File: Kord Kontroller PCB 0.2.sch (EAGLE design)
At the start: 188 parts, among them IC2 74HCT1G125DBV, J1 MIDIOUTB, J2 MIDIOUTA, J3 FTSH-105-01-L-DV-KJ, SW2 SPST_TACT-KMR2, U1 AP2112K-3.3, U2 ATSAMD51J19A-AUT, X3 microUSB

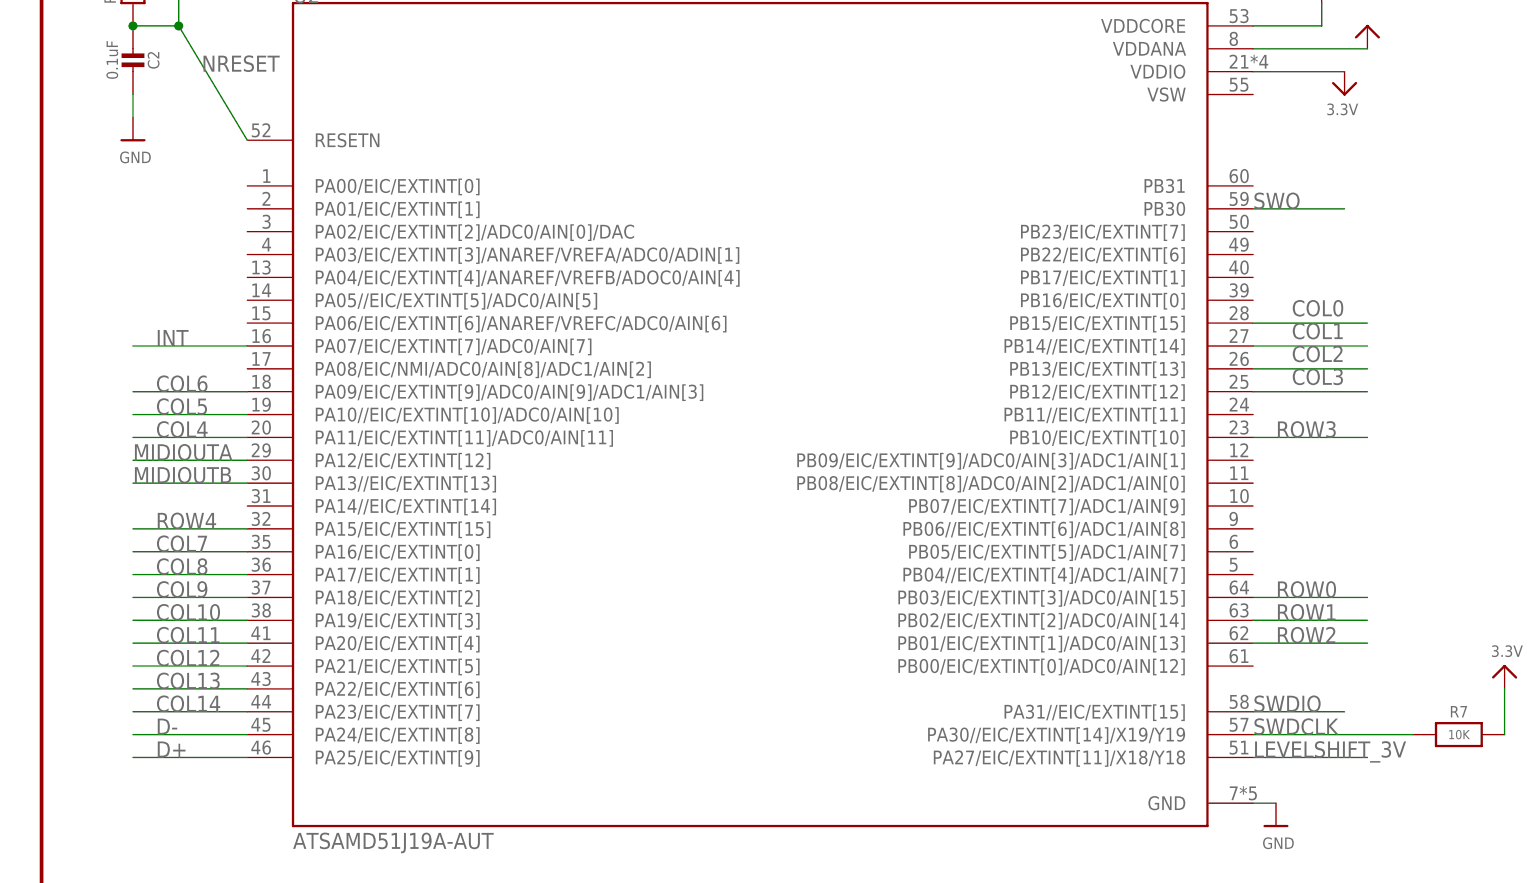
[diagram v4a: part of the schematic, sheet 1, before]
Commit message: Added traces for 7-14
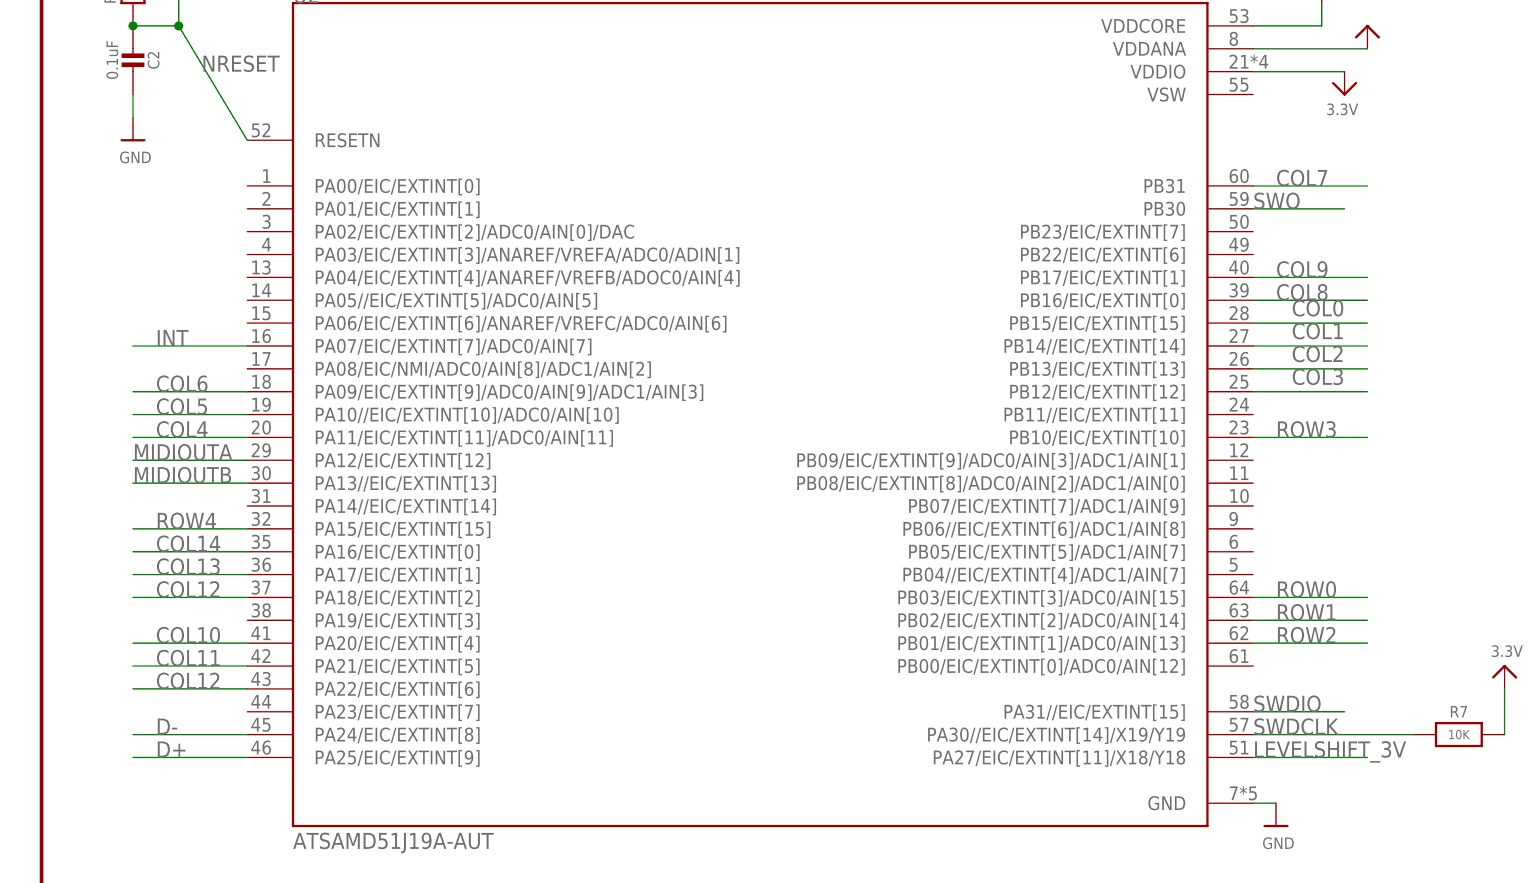
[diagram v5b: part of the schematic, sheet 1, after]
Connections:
- net COL10: now also U2.PA20/EIC/EXTINT[4]; no longer U2.PA19/EIC/EXTINT[3]
- net COL11: now also U2.PA21/EIC/EXTINT[5]; no longer U2.PA20/EIC/EXTINT[4]
- net COL12: now also U2.PA18/EIC/EXTINT[2], U2.PA22/EIC/EXTINT[6]; no longer U2.PA21/EIC/EXTINT[5]
- net COL13: now also U2.PA17/EIC/EXTINT[1]; no longer U2.PA22/EIC/EXTINT[6]
- net COL14: now also U2.PA16/EIC/EXTINT[0]; no longer U2.PA23/EIC/EXTINT[7]
- net COL7: now also B29.P$1, U2.PB31; no longer U2.PA16/EIC/EXTINT[0]
- net COL8: now also U2.PB16/EIC/EXTINT[0]; no longer B29.P$1, U2.PA17/EIC/EXTINT[1]
- net COL9: now also U2.PB17/EIC/EXTINT[1]; no longer U2.PA18/EIC/EXTINT[2]
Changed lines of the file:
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@@
 <net name="COL7" class="0">
 <segment>
-<wire x1="652.78" y1="-63.5" x2="665.48" y2="-63.5" width="0.1524" layer="91"/>
-<label x="655.32" y="-63.5" size="1.778" layer="95"/>
-<pinref part="U2" gate="G$1" pin="PA16/EIC/EXTINT[0]"/>
+<wire x1="777.24" y1="-22.86" x2="789.94" y2="-22.86" width="0.1524" layer="91"/>
+<label x="779.78" y="-22.86" size="1.778" layer="95"/>
+<pinref part="U2" gate="G$1" pin="PB31"/>
 </segment>
 </net>
@@
 <net name="COL8" class="0">
 <segment>
-<wire x1="665.48" y1="-66.04" x2="652.78" y2="-66.04" width="0.1524" layer="91"/>
-<label x="655.32" y="-66.04" size="1.778" layer="95"/>
-<pinref part="U2" gate="G$1" pin="PA17/EIC/EXTINT[1]"/>
+<wire x1="789.94" y1="-35.56" x2="777.24" y2="-35.56" width="0.1524" layer="91"/>
+<label x="779.78" y="-35.56" size="1.778" layer="95"/>
+<pinref part="U2" gate="G$1" pin="PB16/EIC/EXTINT[0]"/>
 </segment>
 </net>
 <net name="COL9" class="0">
+<segment>
+<wire x1="777.24" y1="-33.02" x2="789.94" y2="-33.02" width="0.1524" layer="91"/>
+<label x="779.78" y="-33.02" size="1.778" layer="95"/>
+<pinref part="U2" gate="G$1" pin="PB17/EIC/EXTINT[1]"/>
+</segment>
+</net>
+<net name="COL10" class="0">
+<segment>
+<wire x1="652.78" y1="-73.66" x2="665.48" y2="-73.66" width="0.1524" layer="91"/>
+<label x="655.32" y="-73.66" size="1.778" layer="95"/>
+<pinref part="U2" gate="G$1" pin="PA20/EIC/EXTINT[4]"/>
+</segment>
+</net>
+<net name="COL11" class="0">
+<segment>
+<wire x1="652.78" y1="-76.2" x2="665.48" y2="-76.2" width="0.1524" layer="91"/>
+<label x="655.32" y="-76.2" size="1.778" layer="95"/>
+<pinref part="U2" gate="G$1" pin="PA21/EIC/EXTINT[5]"/>
+</segment>
+</net>
+<net name="COL12" class="0">
 <segment>
 <wire x1="652.78" y1="-68.58" x2="665.48" y2="-68.58" width="0.1524" layer="91"/>
@@
 <pinref part="U2" gate="G$1" pin="PA18/EIC/EXTINT[2]"/>
 </segment>
-</net>
-<net name="COL10" class="0">
-<segment>
-<wire x1="652.78" y1="-71.12" x2="665.48" y2="-71.12" width="0.1524" layer="91"/>
-<label x="655.32" y="-71.12" size="1.778" layer="95"/>
-<pinref part="U2" gate="G$1" pin="PA19/EIC/EXTINT[3]"/>
-</segment>
-</net>
-<net name="COL11" class="0">
-<segment>
-<wire x1="652.78" y1="-73.66" x2="665.48" y2="-73.66" width="0.1524" layer="91"/>
-<label x="655.32" y="-73.66" size="1.778" layer="95"/>
-<pinref part="U2" gate="G$1" pin="PA20/EIC/EXTINT[4]"/>
-</segment>
-</net>
-<net name="COL12" class="0">
-<segment>
-<wire x1="652.78" y1="-76.2" x2="665.48" y2="-76.2" width="0.1524" layer="91"/>
-<label x="655.32" y="-76.2" size="1.778" layer="95"/>
-<pinref part="U2" gate="G$1" pin="PA21/EIC/EXTINT[5]"/>
-</segment>
-</net>
-<net name="COL13" class="0">
 <segment>
 <wire x1="652.78" y1="-78.74" x2="665.48" y2="-78.74" width="0.1524" layer="91"/>
@@
 </segment>
 </net>
+<net name="COL13" class="0">
+<segment>
+<wire x1="652.78" y1="-66.04" x2="665.48" y2="-66.04" width="0.1524" layer="91"/>
+<label x="655.32" y="-66.04" size="1.778" layer="95"/>
+<pinref part="U2" gate="G$1" pin="PA17/EIC/EXTINT[1]"/>
+</segment>
+</net>
 <net name="COL14" class="0">
 <segment>
-<wire x1="652.78" y1="-81.28" x2="665.48" y2="-81.28" width="0.1524" layer="91"/>
-<label x="655.32" y="-81.28" size="1.778" layer="95"/>
-<pinref part="U2" gate="G$1" pin="PA23/EIC/EXTINT[7]"/>
+<wire x1="652.78" y1="-63.5" x2="665.48" y2="-63.5" width="0.1524" layer="91"/>
+<label x="655.32" y="-63.5" size="1.778" layer="95"/>
+<pinref part="U2" gate="G$1" pin="PA16/EIC/EXTINT[0]"/>
 </segment>
 </net>
@@
 <pinref part="B28" gate="G$1" pin="P$1"/>
 <junction x="139.7" y="193.04"/>
+<wire x1="170.18" y1="193.04" x2="185.42" y2="193.04" width="0.1524" layer="91"/>
+<junction x="170.18" y="193.04"/>
+<pinref part="B29" gate="G$1" pin="P$1"/>
+<wire x1="185.42" y1="198.12" x2="185.42" y2="193.04" width="0.1524" layer="91"/>
 </segment>
 </net>
@@
 <wire x1="147.32" y1="198.12" x2="147.32" y2="187.96" width="0.1524" layer="91"/>
 <junction x="147.32" y="187.96"/>
-<pinref part="B29" gate="G$1" pin="P$1"/>
-<wire x1="185.42" y1="198.12" x2="185.42" y2="187.96" width="0.1524" layer="91"/>
-<wire x1="185.42" y1="187.96" x2="177.8" y2="187.96" width="0.1524" layer="91"/>
-<junction x="177.8" y="187.96"/>
-</segment>
-</net>
+</segment>
+</net>

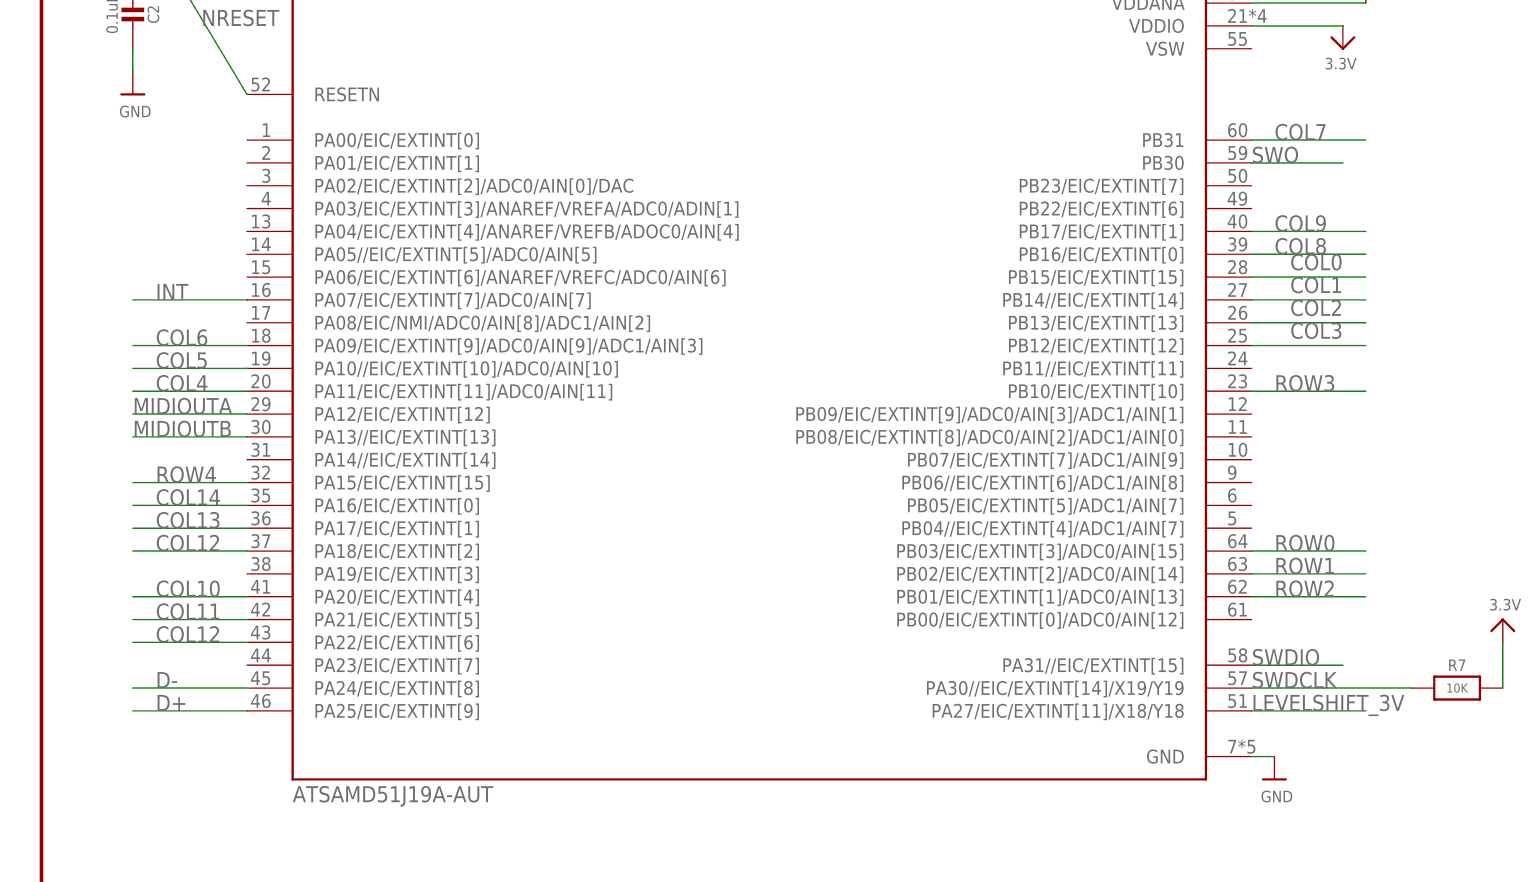
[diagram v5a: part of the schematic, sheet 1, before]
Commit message: routed power and midi
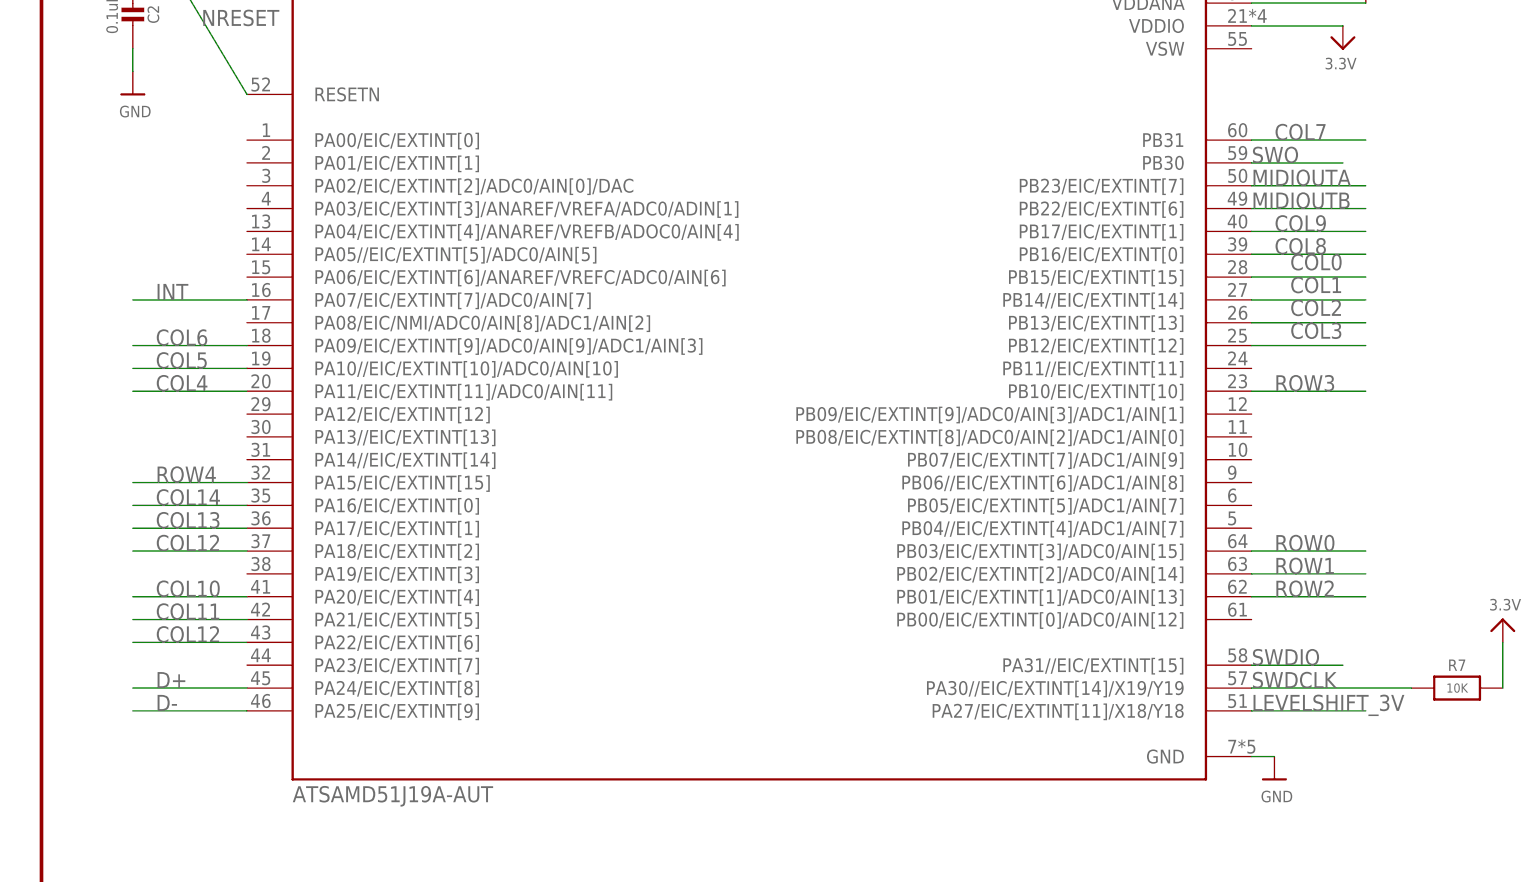
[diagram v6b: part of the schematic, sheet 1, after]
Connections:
- net D+: now also U2.PA24/EIC/EXTINT[8]; no longer U2.PA25/EIC/EXTINT[9]
- net D-: now also U2.PA25/EIC/EXTINT[9]; no longer U2.PA24/EIC/EXTINT[8]
- net MIDIOUTA: now also U2.PB23/EIC/EXTINT[7]; no longer U2.PA12/EIC/EXTINT[12]
- net MIDIOUTB: now also U2.PB22/EIC/EXTINT[6]; no longer U2.PA13//EIC/EXTINT[13]
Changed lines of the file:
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@@
 </segment>
 <segment>
-<wire x1="665.48" y1="-86.36" x2="652.78" y2="-86.36" width="0.1524" layer="91"/>
-<label x="655.32" y="-86.36" size="1.778" layer="95"/>
-<pinref part="U2" gate="G$1" pin="PA25/EIC/EXTINT[9]"/>
+<wire x1="665.48" y1="-83.82" x2="652.78" y2="-83.82" width="0.1524" layer="91"/>
+<label x="655.32" y="-83.82" size="1.778" layer="95"/>
+<pinref part="U2" gate="G$1" pin="PA24/EIC/EXTINT[8]"/>
 </segment>
 </net>
@@
 </segment>
 <segment>
-<wire x1="652.78" y1="-83.82" x2="665.48" y2="-83.82" width="0.1524" layer="91"/>
-<label x="655.32" y="-83.82" size="1.778" layer="95"/>
-<pinref part="U2" gate="G$1" pin="PA24/EIC/EXTINT[8]"/>
+<wire x1="652.78" y1="-86.36" x2="665.48" y2="-86.36" width="0.1524" layer="91"/>
+<label x="655.32" y="-86.36" size="1.778" layer="95"/>
+<pinref part="U2" gate="G$1" pin="PA25/EIC/EXTINT[9]"/>
 </segment>
 </net>
@@
 </segment>
 <segment>
-<wire x1="652.78" y1="-53.34" x2="665.48" y2="-53.34" width="0.1524" layer="91"/>
-<label x="652.78" y="-53.34" size="1.778" layer="95"/>
-<pinref part="U2" gate="G$1" pin="PA12/EIC/EXTINT[12]"/>
+<wire x1="777.24" y1="-27.94" x2="789.94" y2="-27.94" width="0.1524" layer="91"/>
+<label x="777.24" y="-27.94" size="1.778" layer="95"/>
+<pinref part="U2" gate="G$1" pin="PB23/EIC/EXTINT[7]"/>
 </segment>
 </net>
@@
 </segment>
 <segment>
-<wire x1="652.78" y1="-55.88" x2="665.48" y2="-55.88" width="0.1524" layer="91"/>
-<label x="652.78" y="-55.88" size="1.778" layer="95"/>
-<pinref part="U2" gate="G$1" pin="PA13//EIC/EXTINT[13]"/>
+<wire x1="777.24" y1="-30.48" x2="789.94" y2="-30.48" width="0.1524" layer="91"/>
+<label x="777.24" y="-30.48" size="1.778" layer="95"/>
+<pinref part="U2" gate="G$1" pin="PB22/EIC/EXTINT[6]"/>
 </segment>
 </net>

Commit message: Added VDD plane and GND plane
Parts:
- removed FRAME1: FRAME-LEDGER, SparkFun-Aesthetics:FRAME-LEDGER
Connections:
- net COL12: no longer U2.PA18/EIC/EXTINT[2]
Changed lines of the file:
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@@
 <part name="GND18" library="supply1" deviceset="GND" device=""/>
 <part name="GND19" library="supply1" deviceset="GND" device=""/>
-<part name="FRAME1" library="SparkFun-Aesthetics" deviceset="FRAME-LEDGER" device=""/>
 <part name="D25" library="microbuilder" deviceset="DIODE" device="SOD-323" value="1N4148"/>
 <part name="D33" library="microbuilder" deviceset="DIODE" device="SOD-323" value="1N4148"/>
@@
 <attribute name="VALUE" x="706.12" y="55.88" size="1.778" layer="96"/>
 </instance>
-<instance part="FRAME1" gate="G$1" x="642.62" y="-106.68" smashed="yes"/>
-<instance part="FRAME1" gate="G$2" x="972.82" y="-106.68" smashed="yes">
-<attribute name="LAST_DATE_TIME" x="985.52" y="-105.41" size="2.54" layer="94" font="vector"/>
-<attribute name="SHEET" x="1059.18" y="-105.41" size="2.54" layer="94" font="vector"/>
-<attribute name="DRAWING_NAME" x="988.314" y="-88.9" size="2.7432" layer="94" font="vector"/>
-<attribute name="DESIGNER" x="995.934" y="-95.504" size="2.7432" layer="94" font="vector"/>
-<attribute name="REV" x="1061.72" y="-100.076" size="2.7432" layer="94" font="vector"/>
-</instance>
 <instance part="R5" gate="G$1" x="835.66" y="78.74" smashed="yes">
 <attribute name="NAME" x="831.85" y="80.2386" size="1.778" layer="95"/>
@@
 <net name="COL12" class="0">
 <segment>
-<wire x1="652.78" y1="-68.58" x2="665.48" y2="-68.58" width="0.1524" layer="91"/>
-<label x="655.32" y="-68.58" size="1.778" layer="95"/>
-<pinref part="U2" gate="G$1" pin="PA18/EIC/EXTINT[2]"/>
-</segment>
-<segment>
 <wire x1="652.78" y1="-78.74" x2="665.48" y2="-78.74" width="0.1524" layer="91"/>

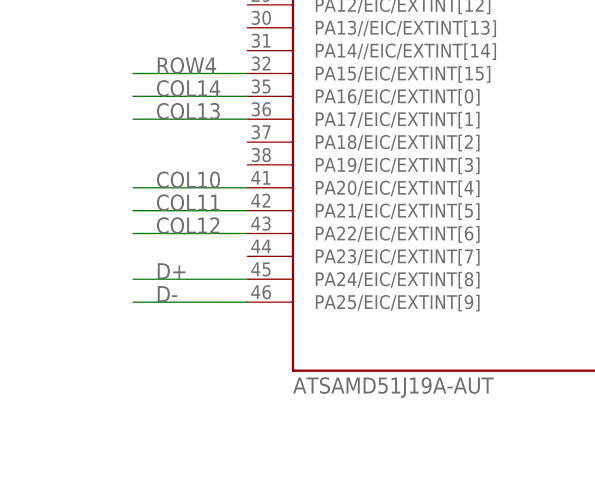
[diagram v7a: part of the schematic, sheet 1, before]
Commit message: Switched pieces to bottom
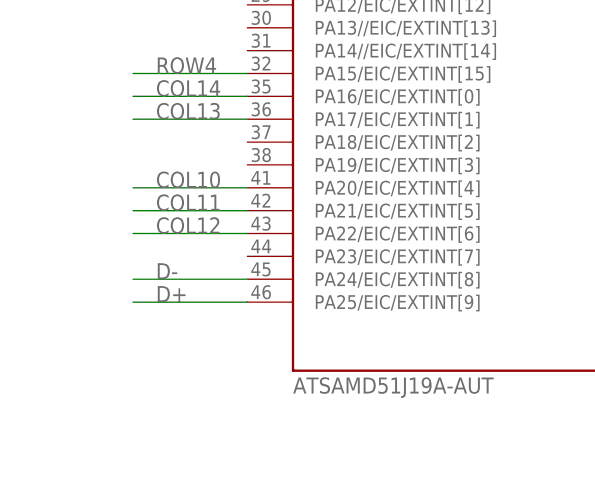
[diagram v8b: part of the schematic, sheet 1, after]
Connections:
- net D+: now also U2.PA25/EIC/EXTINT[9]; no longer U2.PA24/EIC/EXTINT[8]
- net D-: now also U2.PA24/EIC/EXTINT[8]; no longer U2.PA25/EIC/EXTINT[9]
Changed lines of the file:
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@@
 </segment>
 <segment>
-<wire x1="665.48" y1="-83.82" x2="652.78" y2="-83.82" width="0.1524" layer="91"/>
-<label x="655.32" y="-83.82" size="1.778" layer="95"/>
-<pinref part="U2" gate="G$1" pin="PA24/EIC/EXTINT[8]"/>
+<wire x1="665.48" y1="-86.36" x2="652.78" y2="-86.36" width="0.1524" layer="91"/>
+<label x="655.32" y="-86.36" size="1.778" layer="95"/>
+<pinref part="U2" gate="G$1" pin="PA25/EIC/EXTINT[9]"/>
 </segment>
 </net>
@@
 </segment>
 <segment>
-<wire x1="652.78" y1="-86.36" x2="665.48" y2="-86.36" width="0.1524" layer="91"/>
-<label x="655.32" y="-86.36" size="1.778" layer="95"/>
-<pinref part="U2" gate="G$1" pin="PA25/EIC/EXTINT[9]"/>
+<wire x1="652.78" y1="-83.82" x2="665.48" y2="-83.82" width="0.1524" layer="91"/>
+<label x="655.32" y="-83.82" size="1.778" layer="95"/>
+<pinref part="U2" gate="G$1" pin="PA24/EIC/EXTINT[8]"/>
 </segment>
 </net>
